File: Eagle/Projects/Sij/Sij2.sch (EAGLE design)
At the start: 159 parts, among them M1 -30V

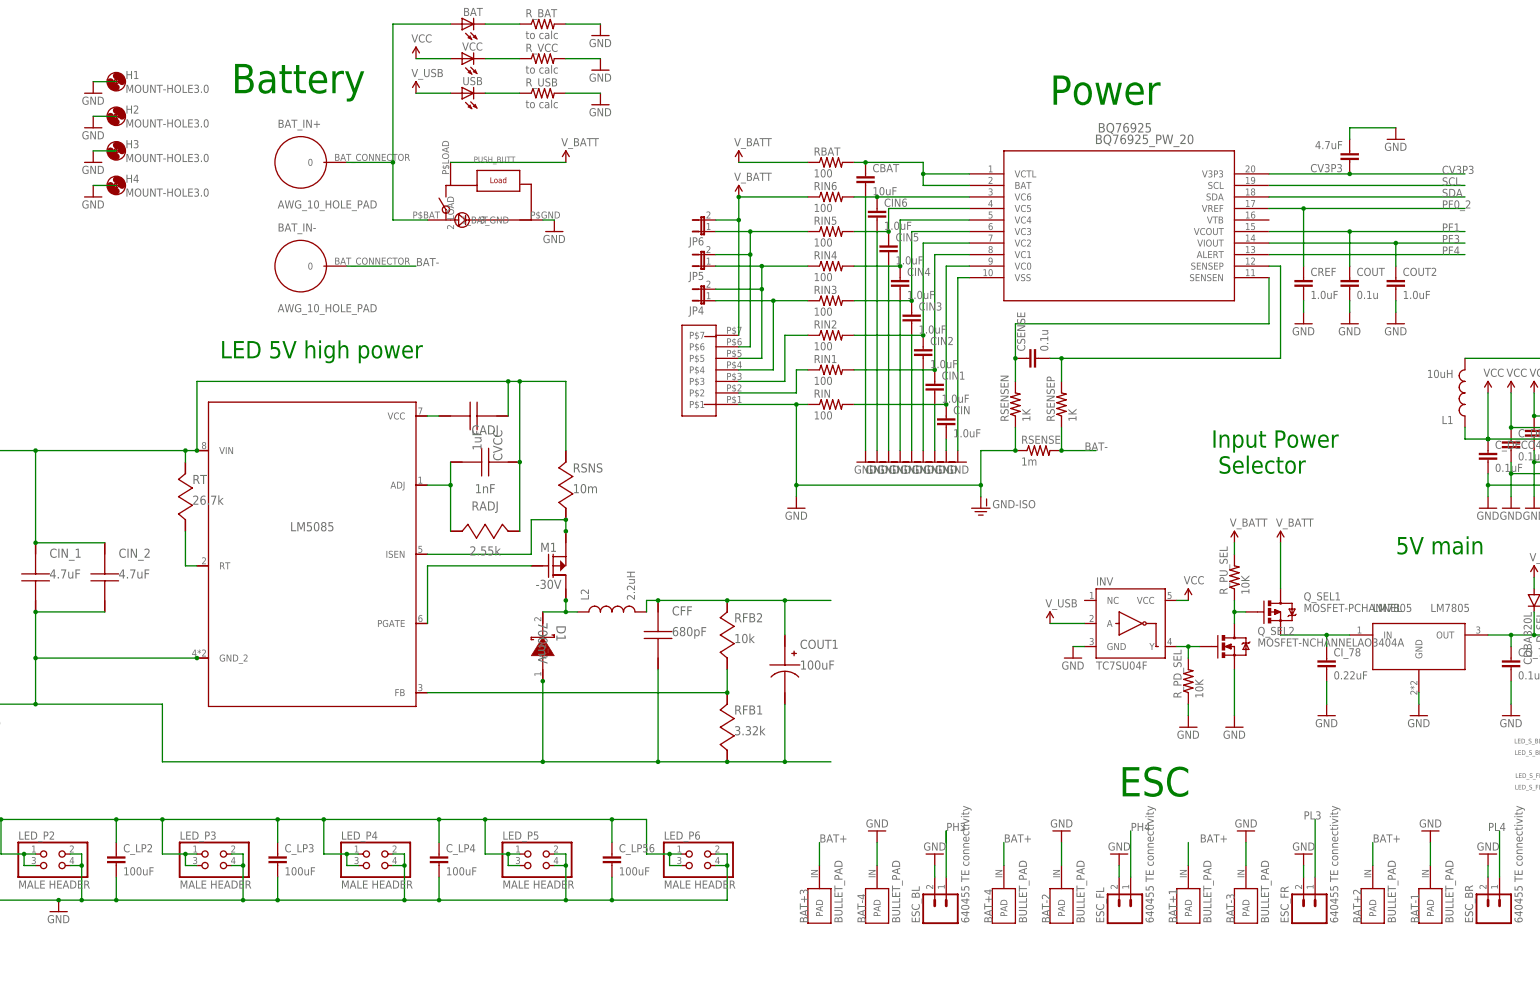
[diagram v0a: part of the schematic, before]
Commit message: Added code for I2C and IMU
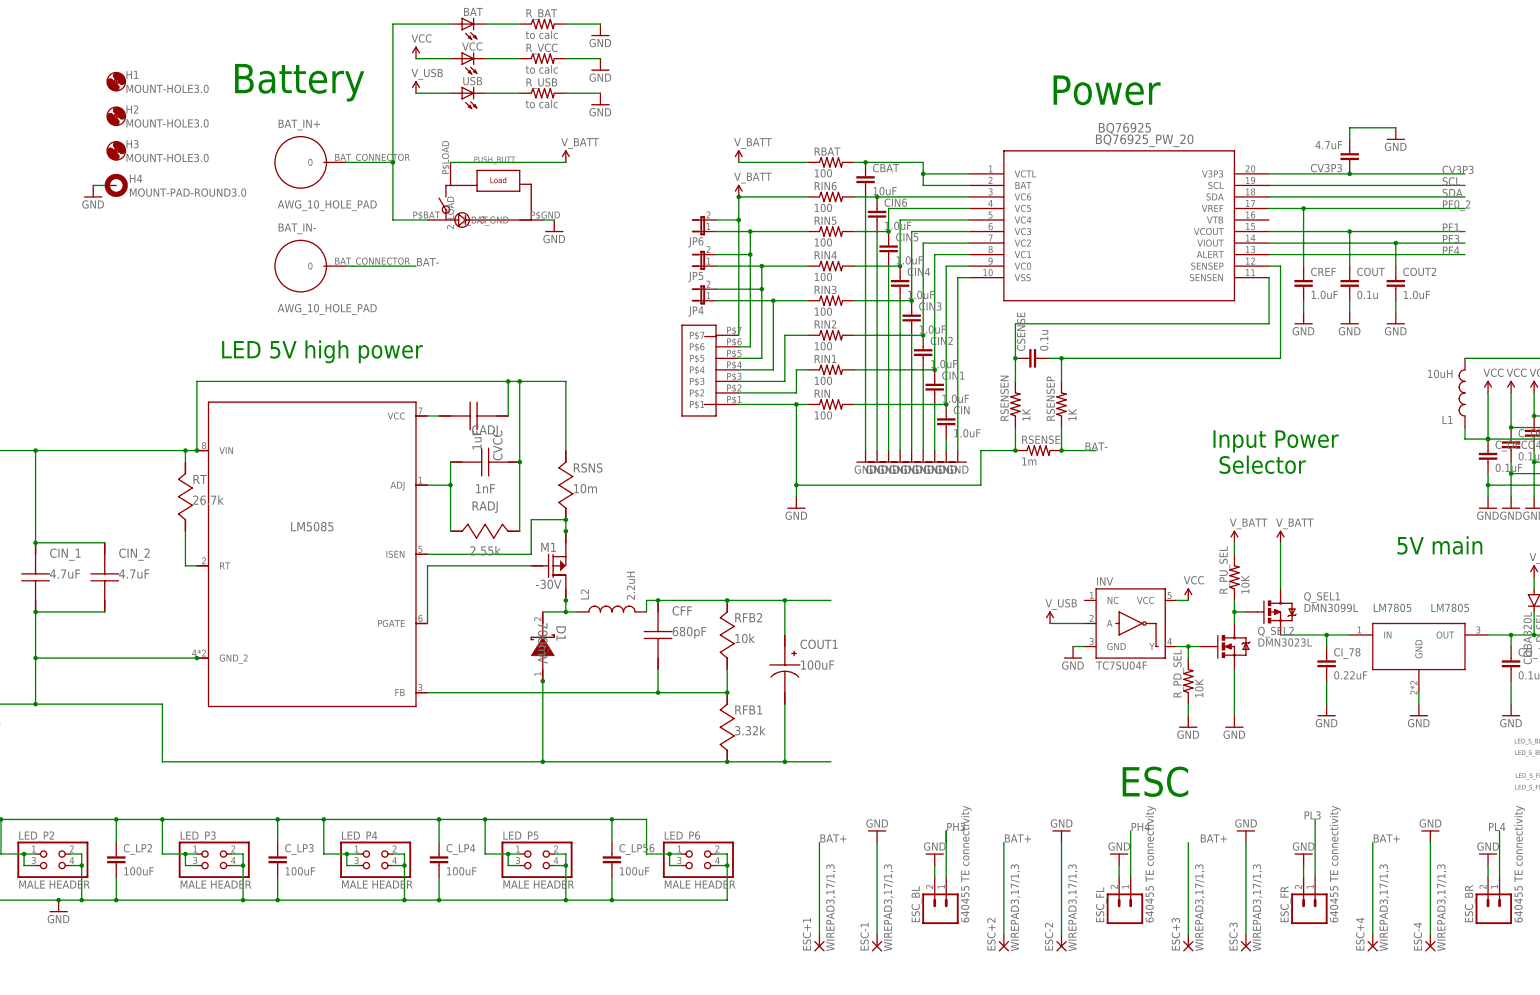
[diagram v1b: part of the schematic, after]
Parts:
- removed BAT+1, BAT+2, BAT+3, BAT+4, BAT-1, BAT-2, BAT-3, BAT-4: BULLET_PAD, custom_parts:BULLET_PAD
- added ESC+1, ESC+2, ESC+3, ESC+4, ESC-1, ESC-2, ESC-3, ESC-4: WIREPAD3,17/1,3, wirepad:WIREPAD3,17/1,3
- 16MHZ: DATASHEET (none) -> https://cdn-shop.adafruit.com/product-files/2215/2215datash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
- BAT_IN+, BAT_IN-: AWG_RATING (none) -> 12
- D_PD_RES, D_PU_RES: DATASHEET (none) -> http://www.diodes.com/_files/datasheets/ds28002.pdf; DIGIKEY (none) -> http://www.digikey.ca/product-detail/en/diodes-incorporated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
- D_SEL: DATASHEET (none) -> http://www.comchiptech.com/cms/UserFiles/CDBA320L-G%20Thru0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
- H4: value MOUNT-HOLE3.0 -> MOUNT-PAD-ROUND3.0; device holes:MOUNT-HOLE3.0 -> holes:MOUNT-PAD-ROUND3.0
- INV: DATASHEET (none) -> http://www.digikey.com/product-detail/en/toshiba-semiconduc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
- L1: DATASHEET (none) -> http://www.yuden.co.jp/productdata/catalog/en/wound01_e.pdf; DIGIKEY (none) -> http://www.digikey.ca/product-detail/en/taiyo-yuden/LBR2012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
- LM7805: DATASHEET (none) -> pdf
- PUSH_BUTT: AWG_RATING (none) -> 16; DATASHEET (none) -> http://media.digikey.com/pdf/Data%20Sheets/CW%20Industries%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; DIGIKEY (none) -> http://www.digikey.ca/product-detail/en/cw-industries/GPB55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
- Q_SEL1: value MOSFET-PCHANNEL -> DMN3099L; DATASHEET (none) -> http://www.diodes.com/_files/datasheets/DMP3099L.pdf
- Q_SEL2: value MOSFET-NCHANNELAO3404A -> DMN3023L; DATASHEET (none) -> http://www.diodes.com/_files/datasheets/DMN3023L.pdf
- RADIO_CONTROLLER: DIGIKEY (none) -> http://www.digikey.ca/product-search/en?mpart=S7B-XH-A%28LF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
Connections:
- net BAT+: now also ESC+1.P, ESC+2.P, ESC+3.P, ESC+4.P; no longer BAT+1.PAD, BAT+2.PAD, BAT+3.PAD, BAT+4.PAD
- net FB_5085: now also CFF.2
- net GND: now also ESC-1.P, ESC-2.P, ESC-3.P, ESC-4.P, H4.MOUNT; no longer BAT-1.PAD, BAT-2.PAD, BAT-3.PAD, BAT-4.PAD, CFF.2
